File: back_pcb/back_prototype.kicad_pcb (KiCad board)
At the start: 2 copper layers, 40 x 100 mm, 80 parts, among them P1 EXPANSION_LEFT, P10 CONN_01X08, P2 EXPANSION_BOTTOM, P3 EXPANSION_TOP, P4 USB_A, P5 AUDIO_CONN, P6 ATMEGA_HEADER, P7 EXPANSION_BOTTOM2, P8 JST, P9 USB_A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

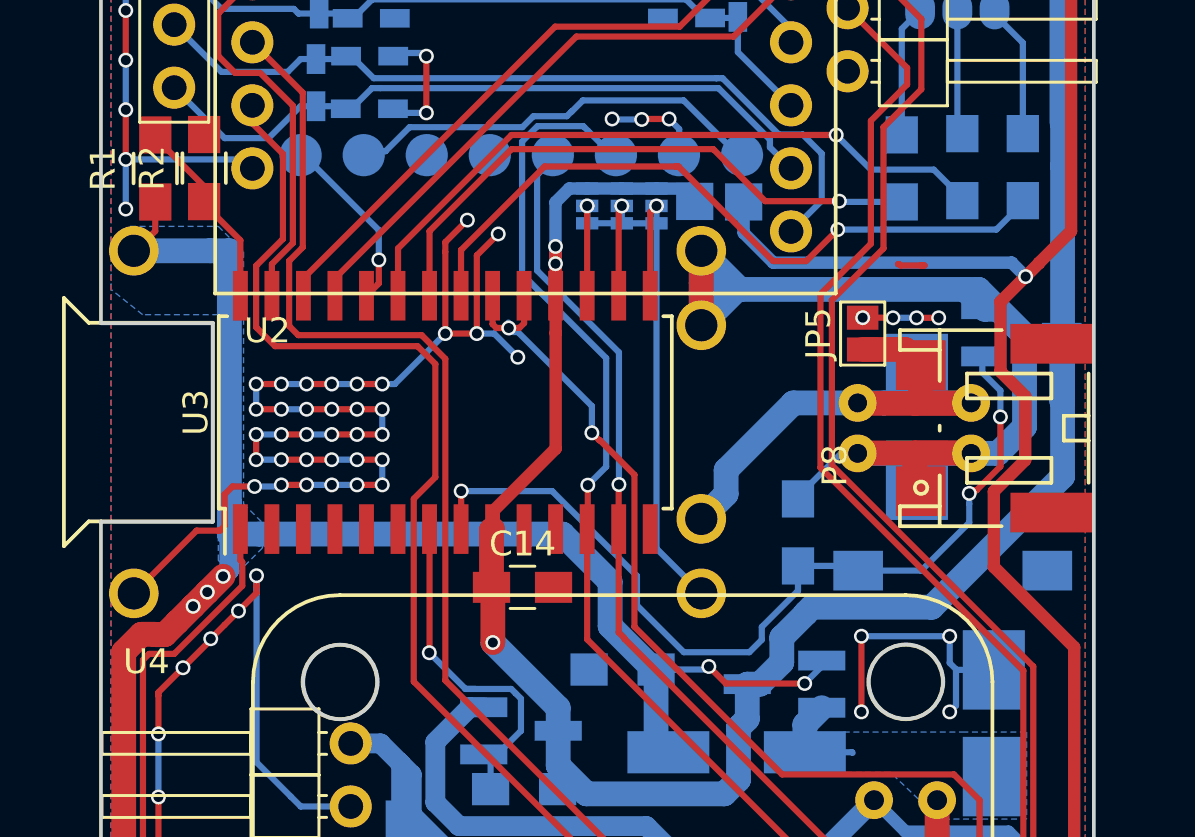
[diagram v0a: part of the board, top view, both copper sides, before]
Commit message: Fixed protection footprint
More like "fucked shit up because Chinese modules"
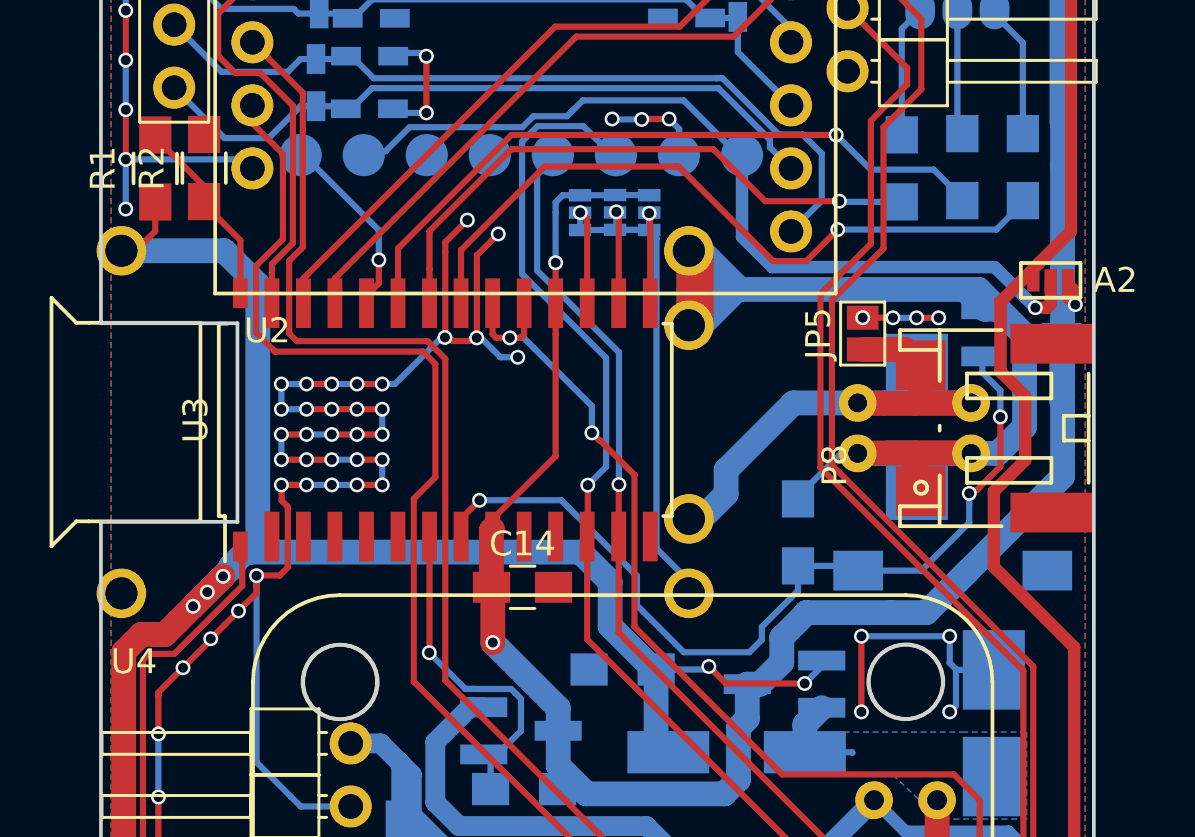
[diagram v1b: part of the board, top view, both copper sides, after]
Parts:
- removed W5: 3V3, Measurement_Points:Measurement_Point_Square-SMD-Pad_Small
- removed W7: VBAT, Measurement_Points:Measurement_Point_Square-SMD-Pad_Small
- added JP8: A2, common-footprints:GS3_SMALL, F.Cu at (79.8, 62.4)
- moved U4 0.50 mm to (54.0, 68.1)
- moved JP3 0.40 mm to (63.6, 59.6)
- moved JP4 0.39 mm to (60.8, 59.6)
- moved JP6 0.38 mm to (62.2, 59.6)
- moved U3 0.30 mm to (55.4, 68.0)
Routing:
- net Net-(JP8-Pad2): track 17.1 -> 35.1 mm, vias 0 -> 1
- net +3V3: track 196.4 -> 183.8 mm, vias 2 -> 1
- net GND: track 362.8 -> 354.7 mm, vias 154 -> 149
- net BATT+: track 47.1 -> 53.1 mm
- net +BATT: track 142.0 -> 144.3 mm
- net VDD: track 115.5 -> 117.5 mm
- net (no net): track 1.24 -> 0.00 mm
- net RTC_ALARM: track 64.6 -> 63.9 mm
- net VBAT_EN: track 36.3 -> 35.7 mm
- net MCP_INT: track 73.6 -> 73.1 mm
- removed copper zone on B.Cu, net VDD
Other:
- outline, holes or cut-outs redrawn

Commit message: Added fiducials to back board (forgot them? Merge conflict?)
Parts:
- added REF**: Fiducial_1mm_Dia_2.54mm_Outer_CopperTop, Fiducials:Fiducial_1mm_Dia_2.54mm_Outer_CopperTop, F.Cu at (76.8, 58.2)
- added REF**: Fiducial_1mm_Dia_2.54mm_Outer_CopperBottom, Fiducials:Fiducial_1mm_Dia_2.54mm_Outer_CopperBottom, F.Cu at (44.8, 43.9)
- added REF**: Fiducial_1mm_Dia_2.54mm_Outer_CopperTop, Fiducials:Fiducial_1mm_Dia_2.54mm_Outer_CopperTop, F.Cu at (44.8, 43.9)
- added REF**: Fiducial_1mm_Dia_2.54mm_Outer_CopperTop, Fiducials:Fiducial_1mm_Dia_2.54mm_Outer_CopperTop, F.Cu at (51.6, 133.2)
- added REF**: Fiducial_1mm_Dia_2.54mm_Outer_CopperBottom, Fiducials:Fiducial_1mm_Dia_2.54mm_Outer_CopperBottom, F.Cu at (44.6, 136.6)
- added REF**: Fiducial_1mm_Dia_2.54mm_Outer_CopperBottom, Fiducials:Fiducial_1mm_Dia_2.54mm_Outer_CopperBottom, F.Cu at (78.8, 134.4)
- added REF**: Fiducial_1mm_Dia_2.54mm_Outer_CopperTop, Fiducials:Fiducial_1mm_Dia_2.54mm_Outer_CopperTop, F.Cu at (78.8, 134.4)
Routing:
- net GND: track 354.7 -> 356.0 mm, vias 149 -> 148
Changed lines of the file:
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@@
 (kicad_pcb (version 4) (host pcbnew 4.0.4-stable)
   (general
-    (links 207)
+    (links 0)
     (no_connects 3)
     (area 41.424999 39.924999 81.575001 140.075001)
@@
     (tracks 1218)
     (zones 0)
-    (modules 79)
+    (modules 86)
     (nets 61)
   )
@@
     (36 B.SilkS user)
     (37 F.SilkS user)
-    (38 B.Mask user hide)
-    (39 F.Mask user hide)
+    (38 B.Mask user)
+    (39 F.Mask user)
     (40 Dwgs.User user hide)
     (41 Cmts.User user hide)
@@
     (mod_text_size 1 1)
     (mod_text_width 0.15)
-    (pad_size 1.2 0.6)
+    (pad_size 1 1)
     (pad_drill 0)
     (pad_to_mask_clearance 0.2)
@@
     (add_net VPP)
   )
+  (module Fiducials:Fiducial_1mm_Dia_2.54mm_Outer_CopperTop (layer F.Cu)
+    (at 76.85 58.2)
+    (descr "Circular Fiducial, 1mm bare copper top; 2.54mm keepout")
+    (tags marker)
+    (attr virtual)
+    (fp_text reference REF** (at 3.4 0.7) (layer F.SilkS)
+      (effects (font (size 1 1) (thickness 0.15)))
+    )
+    (fp_text value Fiducial_1mm_Dia_2.54mm_Outer_CopperTop (at 0 -1.8) (layer F.Fab)
+      (effects (font (size 1 1) (thickness 0.15)))
+    )
+    (fp_circle (center 0 0) (end 1.55 0) (layer F.CrtYd) (width 0.05))
+    (pad ~ smd circle (at 0 0) (size 1 1) (layers F.Cu F.Mask)
+      (solder_mask_margin 0.77) (clearance 0.77))
+  )
+  (module Fiducials:Fiducial_1mm_Dia_2.54mm_Outer_CopperBottom (layer F.Cu)
+    (at 44.8 43.9)
+    (descr "Circular Fiducial, 1mm bare copper bottom; 2.54mm keepout")
+    (tags marker)
+    (attr virtual)
+    (fp_text reference REF** (at 3.4 0.7) (layer F.SilkS)
+      (effects (font (size 1 1) (thickness 0.15)))
+    )
+    (fp_text value Fiducial_1mm_Dia_2.54mm_Outer_CopperBottom (at 0 -1.8) (layer F.Fab)
+      (effects (font (size 1 1) (thickness 0.15)))
+    )
+    (fp_circle (center 0 0) (end 1.55 0) (layer B.CrtYd) (width 0.05))
+    (pad ~ smd circle (at 0 0) (size 1 1) (layers B.Cu B.Mask)
+      (solder_mask_margin 0.77) (clearance 0.77))
+  )
   (module common-footprints:GS3_SMALL (layer B.Cu)
     (at 62.20968 59.63516)
@@
       (net 1 +3V3))
   )
+  (module Fiducials:Fiducial_1mm_Dia_2.54mm_Outer_CopperTop (layer F.Cu)
+    (at 44.8 43.9)
+    (descr "Circular Fiducial, 1mm bare copper top; 2.54mm keepout")
+    (tags marker)
+    (attr virtual)
+    (fp_text reference REF** (at 3.4 0.7) (layer F.SilkS)
+      (effects (font (size 1 1) (thickness 0.15)))
+    )
+    (fp_text value Fiducial_1mm_Dia_2.54mm_Outer_CopperTop (at 0 -1.8) (layer F.Fab)
+      (effects (font (size 1 1) (thickness 0.15)))
+    )
+    (fp_circle (center 0 0) (end 1.55 0) (layer F.CrtYd) (width 0.05))
+    (pad ~ smd circle (at 0 0) (size 1 1) (layers F.Cu F.Mask)
+      (solder_mask_margin 0.77) (clearance 0.77))
+  )
+  (module Fiducials:Fiducial_1mm_Dia_2.54mm_Outer_CopperTop (layer F.Cu)
+    (at 51.6 133.25)
+    (descr "Circular Fiducial, 1mm bare copper top; 2.54mm keepout")
+    (tags marker)
+    (attr virtual)
+    (fp_text reference REF** (at 3.4 0.7) (layer F.SilkS)
+      (effects (font (size 1 1) (thickness 0.15)))
+    )
+    (fp_text value Fiducial_1mm_Dia_2.54mm_Outer_CopperTop (at 0 -1.8) (layer F.Fab)
+      (effects (font (size 1 1) (thickness 0.15)))
+    )
+    (fp_circle (center 0 0) (end 1.55 0) (layer F.CrtYd) (width 0.05))
+    (pad ~ smd circle (at 0 0) (size 1 1) (layers F.Cu F.Mask)
+      (solder_mask_margin 0.77) (clearance 0.77))
+  )
+  (module Fiducials:Fiducial_1mm_Dia_2.54mm_Outer_CopperBottom (layer F.Cu)
+    (at 44.6 136.6)
+    (descr "Circular Fiducial, 1mm bare copper bottom; 2.54mm keepout")
+    (tags marker)
+    (attr virtual)
+    (fp_text reference REF** (at 3.4 0.7) (layer F.SilkS)
+      (effects (font (size 1 1) (thickness 0.15)))
+    )
+    (fp_text value Fiducial_1mm_Dia_2.54mm_Outer_CopperBottom (at 0 -1.8) (layer F.Fab)
+      (effects (font (size 1 1) (thickness 0.15)))
+    )
+    (fp_circle (center 0 0) (end 1.55 0) (layer B.CrtYd) (width 0.05))
+    (pad ~ smd circle (at 0 0) (size 1 1) (layers B.Cu B.Mask)
+      (solder_mask_margin 0.77) (clearance 0.77))
+  )
+  (module Fiducials:Fiducial_1mm_Dia_2.54mm_Outer_CopperBottom (layer F.Cu)
+    (at 78.85 134.4)
+    (descr "Circular Fiducial, 1mm bare copper bottom; 2.54mm keepout")
+    (tags marker)
+    (attr virtual)
+    (fp_text reference REF** (at 3.4 0.7) (layer F.SilkS)
+      (effects (font (size 1 1) (thickness 0.15)))
+    )
+    (fp_text value Fiducial_1mm_Dia_2.54mm_Outer_CopperBottom (at 0 -1.8) (layer F.Fab)
+      (effects (font (size 1 1) (thickness 0.15)))
+    )
+    (fp_circle (center 0 0) (end 1.55 0) (layer B.CrtYd) (width 0.05))
+    (pad ~ smd circle (at 0 0) (size 1 1) (layers B.Cu B.Mask)
+      (solder_mask_margin 0.77) (clearance 0.77))
+  )
+  (module Fiducials:Fiducial_1mm_Dia_2.54mm_Outer_CopperTop (layer F.Cu)
+    (at 78.85 134.4)
+    (descr "Circular Fiducial, 1mm bare copper top; 2.54mm keepout")
+    (tags marker)
+    (attr virtual)
+    (fp_text reference REF** (at 3.4 0.7) (layer F.SilkS)
+      (effects (font (size 1 1) (thickness 0.15)))
+    )
+    (fp_text value Fiducial_1mm_Dia_2.54mm_Outer_CopperTop (at 0 -1.8) (layer F.Fab)
+      (effects (font (size 1 1) (thickness 0.15)))
+    )
+    (fp_circle (center 0 0) (end 1.55 0) (layer F.CrtYd) (width 0.05))
+    (pad ~ smd circle (at 0 0) (size 1 1) (layers F.Cu F.Mask)
+      (solder_mask_margin 0.77) (clearance 0.77))
+  )
   (gr_text "Designed in KiCad" (at 79.2988 109.6772 90) (layer B.SilkS)
     (effects (font (size 1.5 1.5) (thickness 0.3)) (justify mirror))
@@
   (segment (start 70.612 46.101) (end 71.3486 46.101) (width 1) (layer B.Cu) (net 1))
   (segment (start 51.6928 81.2) (end 52.07 80.8228) (width 0.25) (layer B.Cu) (net 1))
+  (segment (start 79.375 136.525) (end 81.03108 134.86892) (width 0.25) (layer B.Cu) (net 2))
+  (segment (start 81.03108 134.86892) (end 81.03108 133.73608) (width 0.25) (layer B.Cu) (net 2))
+  (segment (start 81.03108 133.73608) (end 79.375 132.08) (width 0.25) (layer B.Cu) (net 2))
   (segment (start 63.58382 59.66714) (end 63.58382 60.33516) (width 0.25) (layer B.Cu) (net 2))
   (segment (start 62.26302 59.6138) (end 62.26302 60.28182) (width 0.25) (layer B.Cu) (net 2))
@@
   (segment (start 79.375 132.08) (end 79.375 129.54) (width 0.25) (layer F.Cu) (net 2))
   (via (at 79.375 129.54) (size 0.6) (drill 0.4) (layers F.Cu B.Cu) (net 2))
-  (segment (start 79.375 134.62) (end 79.375 132.08) (width 0.25) (layer B.Cu) (net 2))
   (via (at 79.375 132.08) (size 0.6) (drill 0.4) (layers F.Cu B.Cu) (net 2))
-  (segment (start 79.375 136.525) (end 79.375 134.62) (width 0.25) (layer F.Cu) (net 2))
-  (via (at 79.375 134.62) (size 0.6) (drill 0.4) (layers F.Cu B.Cu) (net 2))
   (segment (start 78.105 137.795) (end 79.375 136.525) (width 0.25) (layer B.Cu) (net 2))
   (via (at 79.375 136.525) (size 0.6) (drill 0.4) (layers F.Cu B.Cu) (net 2))

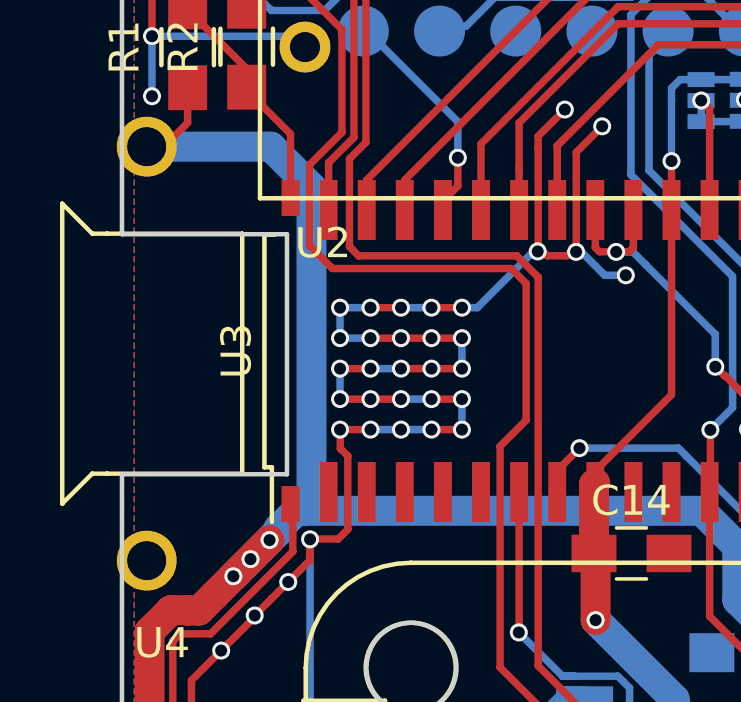
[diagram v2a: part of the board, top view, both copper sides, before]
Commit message: Small fixes
Enlarged GPIO expander pads (where they were made smaller before)
Removed mask near MicroUSB connector to make it possible to solder it to
the board (for worst case of MicroUSB connector being prone to breaking
off)
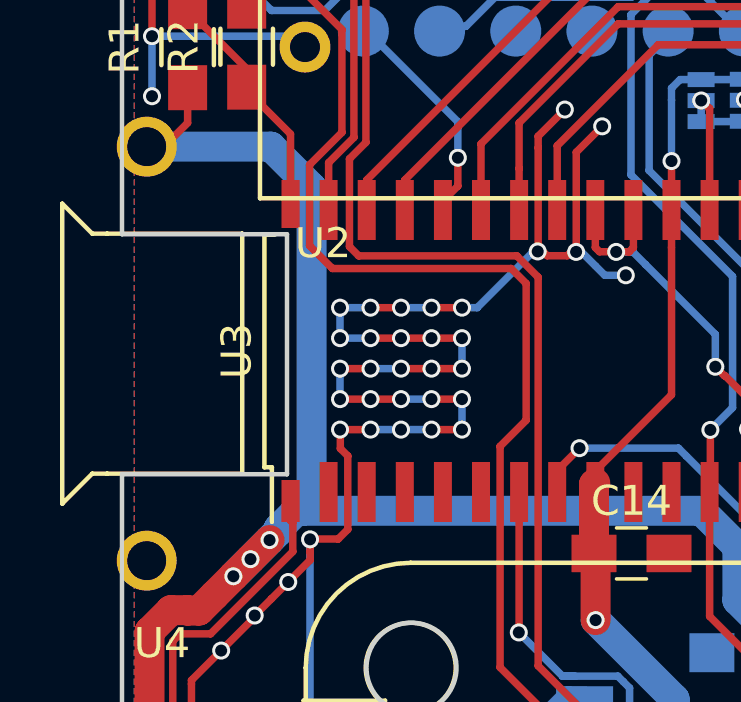
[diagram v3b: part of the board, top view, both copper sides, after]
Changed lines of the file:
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@@
 (kicad_pcb (version 4) (host pcbnew 4.0.4-stable)
   (general
-    (links 0)
+    (links 207)
     (no_connects 3)
-    (area 41.424999 39.924999 81.575001 140.075001)
+    (area 26.354761 37.8762 97.095239 142.393952)
     (thickness 1.6)
     (drawings 26)
@@
     (mod_text_size 1 1)
     (mod_text_width 0.15)
-    (pad_size 1 1)
+    (pad_size 1.6 0.6)
     (pad_drill 0)
     (pad_to_mask_clearance 0.2)
@@
     (fp_line (start -3.875 9.125) (end 3.875 9.125) (layer F.SilkS) (width 0.15))
     (fp_line (start -3.875 -8.875) (end -5.7 -8.875) (layer F.SilkS) (width 0.15))
-    (pad 1 smd rect (at -5.1 -8.255 90) (size 1.2 0.6) (layers F.Cu F.Paste F.Mask)
+    (pad 1 smd rect (at -5 -8.255 90) (size 1.4 0.6) (layers F.Cu F.Paste F.Mask)
       (net 17 RTC_ALARM))
     (pad 2 smd rect (at -4.7 -6.985 90) (size 2 0.6) (layers F.Cu F.Paste F.Mask))
@@
     (pad 27 smd rect (at 4.7 -6.985 90) (size 2 0.6) (layers F.Cu F.Paste F.Mask)
       (net 39 SIM800_RST))
-    (pad 28 smd rect (at 5.1 -8.255 90) (size 1.2 0.6) (layers F.Cu F.Paste F.Mask)
+    (pad 28 smd rect (at 4.9 -8.255 90) (size 1.6 0.6) (layers F.Cu F.Paste F.Mask)
       (net 30 CHARGING_SENSE))
     (model Housings_SOIC.3dshapes/SOIC-28_7.5x17.9mm_Pitch1.27mm.wrl
@@
     (polygon
       (pts
-        (xy 60.07862 59.35472) (xy 64.31788 59.33694) (xy 64.30772 60.37834) (xy 64.0461 60.83554) (xy 64.03594 64.4779)
+        (xy 60.075 59.225) (xy 64.3 59.225) (xy 64.30772 60.37834) (xy 64.0461 60.83554) (xy 64.03594 64.4779)
         (xy 60.57646 64.4779) (xy 60.579 61.595) (xy 60.07608 60.8457)
       )
@@
       )
     )
+  )
+  (zone (net 0) (net_name "") (layer F.Mask) (hatch edge 0.508)
+    (connect_pads (clearance 0.18))
+    (min_thickness 0.254)
+    (fill yes (arc_segments 16) (thermal_gap 0.508) (thermal_bridge_width 0.508))
+    (polygon
+      (pts
+        (xy 41.5 62.7) (xy 45.9 62.7) (xy 45.9 64.1) (xy 41.5 64.1)
+      )
+    )
+  )
+  (zone (net 0) (net_name "") (layer F.Mask) (hatch edge 0.508)
+    (connect_pads (clearance 0.18))
+    (min_thickness 0.254)
+    (fill yes (arc_segments 16) (thermal_gap 0.508) (thermal_bridge_width 0.508))
+    (polygon
+      (pts
+        (xy 41.5 72.1) (xy 45.9 72.1) (xy 45.9 73.9) (xy 41.5 73.9)
+      )
+    )

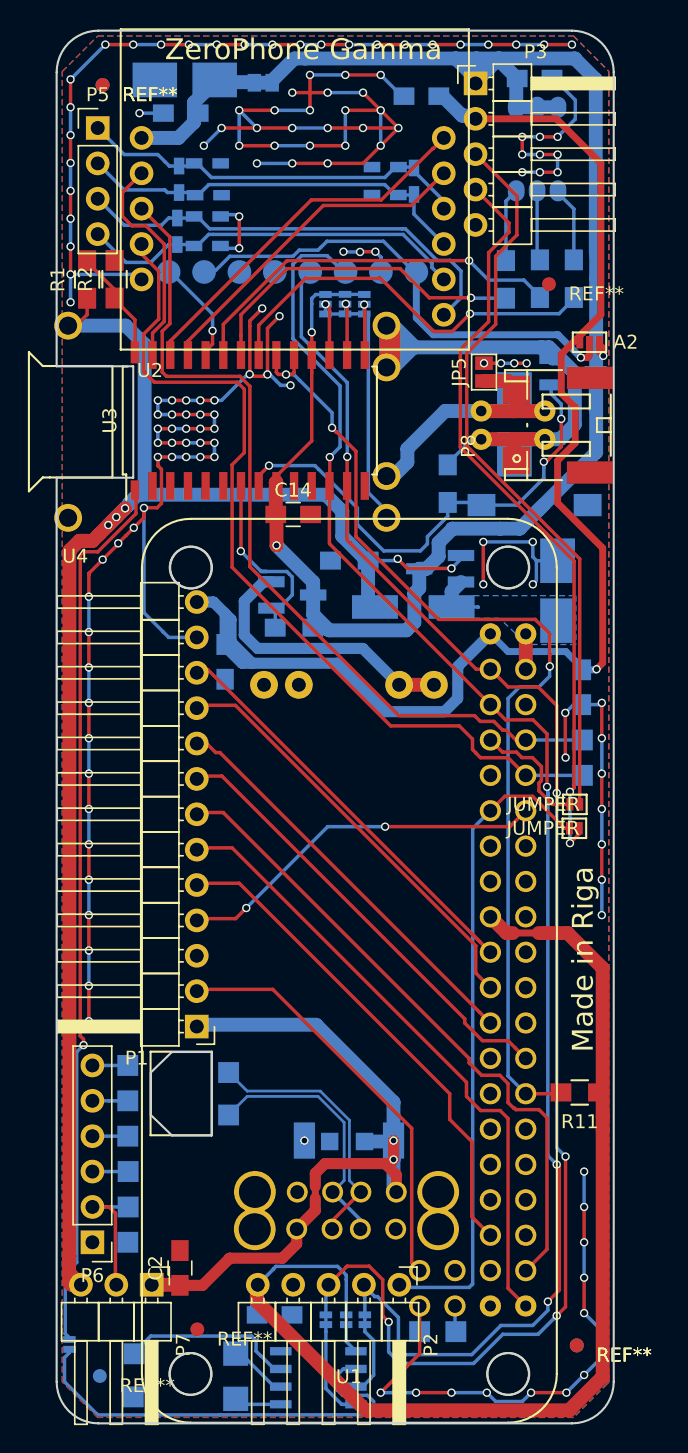
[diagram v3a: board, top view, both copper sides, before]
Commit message: Adjusted solder mask clearance, moved traces that weren't covered
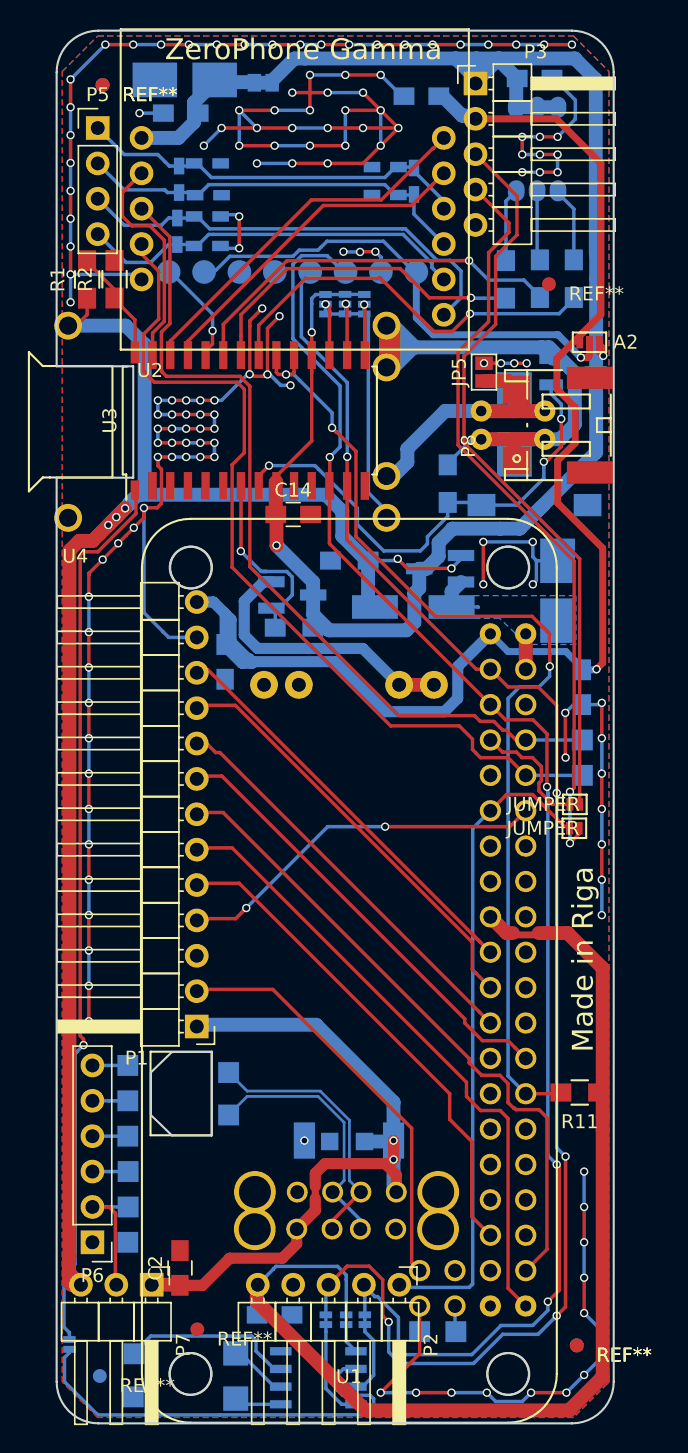
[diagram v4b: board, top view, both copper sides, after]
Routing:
- net +3V3: track 183.8 -> 184.5 mm
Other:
- rule pad_to_mask_clearance: 0.2 -> 0.16
